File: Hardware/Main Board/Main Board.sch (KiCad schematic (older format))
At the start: 43 parts, among them Q1 NPN, Q2 NPN, Q3 A04484, SW1 Momentary, U1 MC33063AD, U2 NCP718A, U3 ATtiny20-CCU

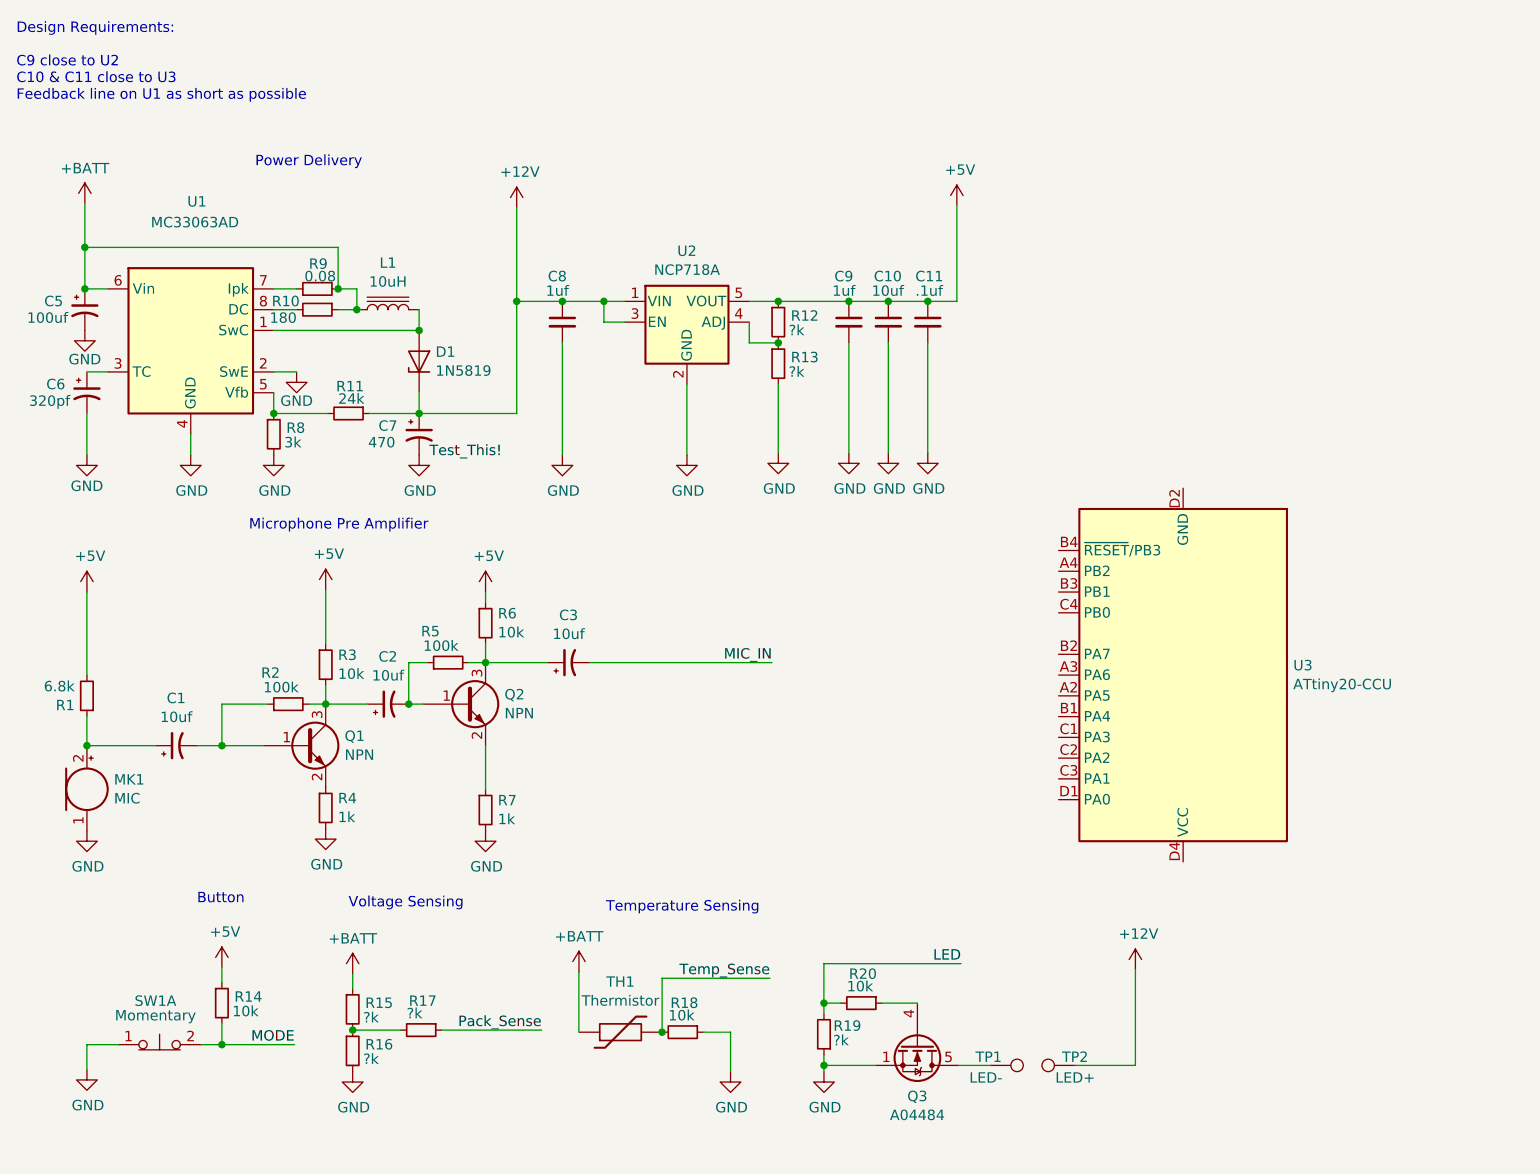
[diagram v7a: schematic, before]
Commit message: Voltage read code, expenses and voltage divider for linear reg update
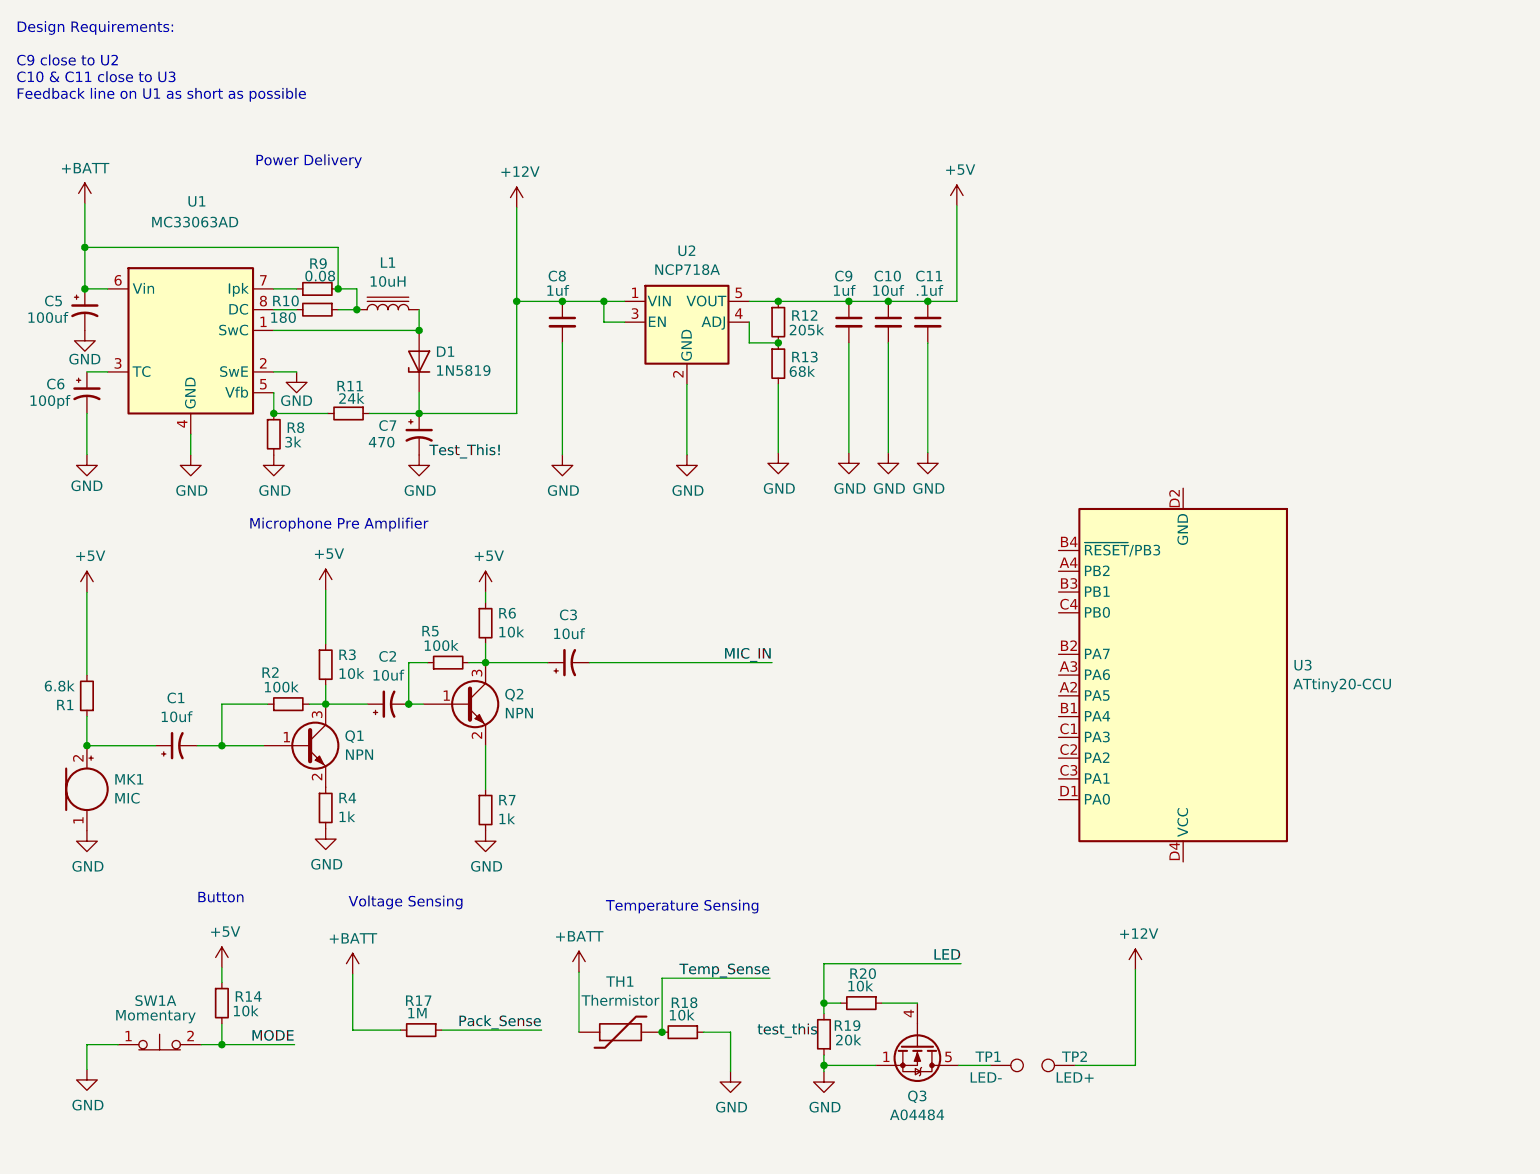
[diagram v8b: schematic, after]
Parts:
- removed R15, R16: ?k, symbol Device:R_Small
- C6: value 320pf -> 100pf
- R12: value ?k -> 205k
- R13: value ?k -> 68k
- R17: value ?k -> 1M
- R19: value ?k -> 20k
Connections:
- net +BATT: now also R17.2
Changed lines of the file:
@@
 P 950 2690
 F 0 "C6" H 800 2730 50  0000 C CNN
-F 1 "320pf" H 770 2650 50  0000 C CNN
+F 1 "100pf" H 770 2650 50  0000 C CNN
 F 2 "" H 950 2690 50  0001 C CNN
 F 3 "~" H 950 2690 50  0001 C CNN
@@
 P 4280 2550
 F 0 "R13" H 4340 2580 50  0000 L CNN
-F 1 "?k" H 4330 2510 50  0000 L CNN
+F 1 "68k" H 4330 2510 50  0000 L CNN
 F 2 "" H 4280 2550 50  0001 C CNN
 F 3 "~" H 4280 2550 50  0001 C CNN
@@
 P 4280 2350
 F 0 "R12" H 4340 2380 50  0000 L CNN
-F 1 "?k" H 4330 2310 50  0000 L CNN
+F 1 "205k" H 4330 2310 50  0000 L CNN
 F 2 "" H 4280 2350 50  0001 C CNN
 F 3 "~" H 4280 2350 50  0001 C CNN
@@
 U 1 1 5EBF9002
 P 2560 5760
-F 0 "R17" V 2420 5700 50  0000 L CNN
-F 1 "?k" V 2480 5690 50  0000 L CNN
+F 0 "R17" V 2420 5680 50  0000 L CNN
+F 1 "1M" V 2480 5690 50  0000 L CNN
 F 2 "" H 2560 5760 50  0001 C CNN
 F 3 "~" H 2560 5760 50  0001 C CNN
@@
 	0    1    1    0
 $EndComp
-Wire Wire Line
-	2230 5490 2230 5560
 Wire Wire Line
 	2460 5760 2230 5760
@@
 P 4500 5780
 F 0 "R19" H 4320 5740 50  0000 L CNN
-F 1 "?k" H 4380 5810 50  0000 L CNN
+F 1 "20k" H 4320 5810 50  0000 L CNN
 F 2 "" H 4500 5780 50  0001 C CNN
 F 3 "~" H 4500 5780 50  0001 C CNN
@@
 	1    0    0    -1
 $EndComp
-$Comp
-L power:GND #PWR021
-U 1 1 5EBF8995
-P 2230 5960
-F 0 "#PWR021" H 2230 5710 50  0001 C CNN
-F 1 "GND" H 2235 5787 50  0000 C CNN
-F 2 "" H 2230 5960 50  0001 C CNN
-F 3 "" H 2230 5960 50  0001 C CNN
-	1    2230 5960
-	1    0    0    -1
-$EndComp
-$Comp
-L Device:R_Small R16
-U 1 1 5EBF86E0
-P 2230 5860
-F 0 "R16" H 2290 5890 50  0000 L CNN
-F 1 "?k" H 2280 5820 50  0000 L CNN
-F 2 "" H 2230 5860 50  0001 C CNN
-F 3 "~" H 2230 5860 50  0001 C CNN
-	1    2230 5860
-	1    0    0    -1
-$EndComp
-Connection ~ 2230 5760
-$Comp
-L Device:R_Small R15
-U 1 1 5EBF785D
-P 2230 5660
-F 0 "R15" H 2290 5690 50  0000 L CNN
-F 1 "?k" H 2280 5620 50  0000 L CNN
-F 2 "" H 2230 5660 50  0001 C CNN
-F 3 "~" H 2230 5660 50  0001 C CNN
-	1    2230 5660
-	1    0    0    -1
-$EndComp
+Wire Wire Line
+	2230 5490 2230 5760
+Text Label 4470 5800 2    50   ~ 0
+test_this
 $EndSCHEMATC
